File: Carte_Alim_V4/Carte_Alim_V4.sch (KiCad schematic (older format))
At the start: 61 parts, among them J1 BAT_IN, J10 12VC, J11 12VC, J12 12VC, J13 12VP, J14 12VP, J15 12VP, J16 12VP, J17 12VP, J18 12VP, J19 5VC, J2 BAT_IN, J20 5V_CAN, J21 5VC, J22 5V_CAN, J23 5VC, J24 5V_CAN, J25 5VC, J26 5V_CAN, J27 5VP, J28 5VP, J29 5VP, J3 MOT_OUT, J30 5VP, J31 5VP, J32 5VP, J4 MOT_OUT, J5 MOT_OUT, J6 MOT_OUT, J7 12VC, J8 12VC, J9 12VC, U1 LM2678S-5.0, U2 LM2678S-12

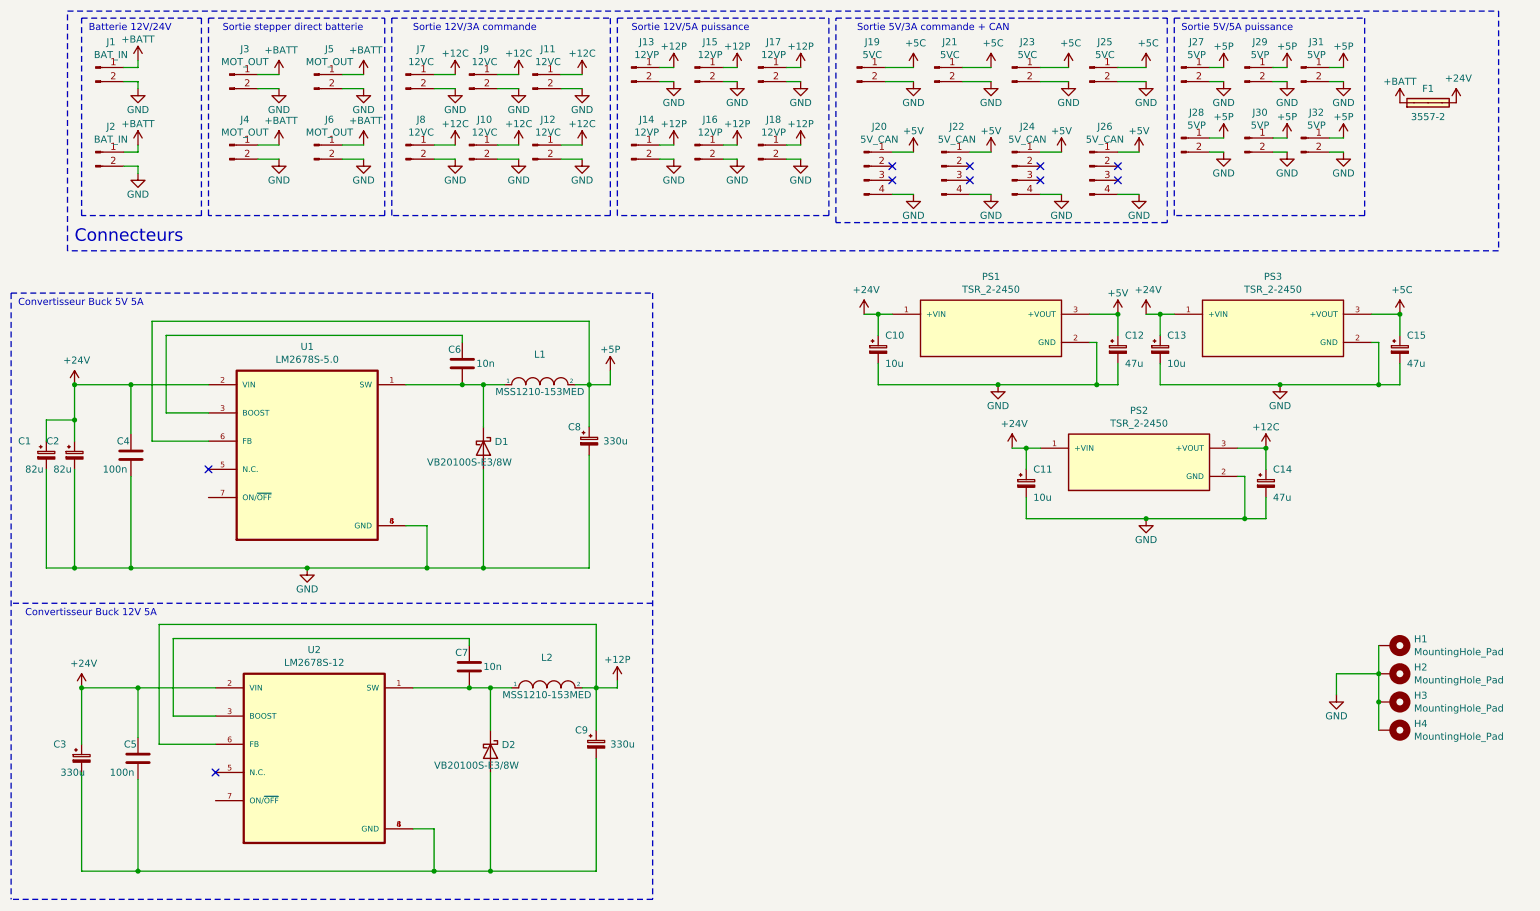
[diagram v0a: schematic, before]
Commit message: IO prete, Pompe finir sérigraphie, Alim+AX12 à faire
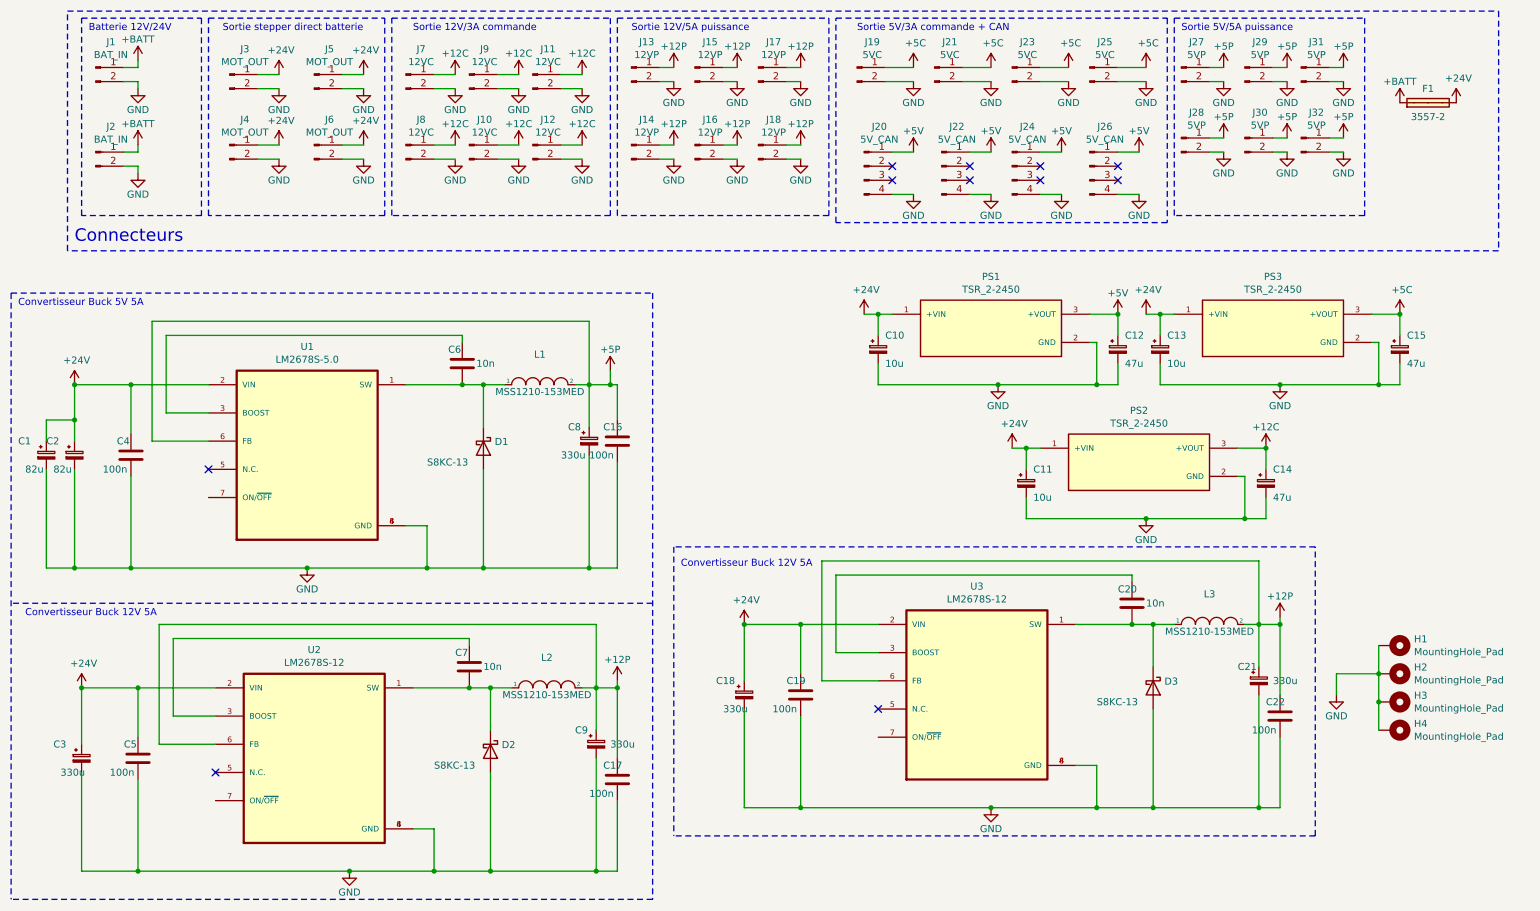
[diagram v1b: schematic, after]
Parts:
- added C16, C17, C19, C22: 100n, Capacitor_SMD:C_0805_2012Metric_Pad1.18x1.45mm_HandSolder, symbol Device:C
- added C18: 330u, Capacitor_SMD:CP_Elec_10x12.6, symbol Device:CP_Small
- added C20: 10n, Capacitor_SMD:C_0805_2012Metric_Pad1.18x1.45mm_HandSolder, symbol Device:C
- added C21: 330u, Capacitor_SMD:CP_Elec_8x6.2, symbol Device:CP_Small
- added D3: S8KC-13, Diode_SMD:D_SMC_Handsoldering, symbol Device:D_Schottky
- added L3: MSS1210-153MED, Inductor_SMD:L_12x12mm_H8mm, symbol pspice:INDUCTOR
- added U3: LM2678S-12, AREA_lib_composant:TO127P1435X464-8N, symbol AREA_composant:LM2678S-12
- D1, D2: value VB20100S-E3/8W -> S8KC-13; footprint Package_TO_SOT_SMD:TO-263-2_TabPin1 -> Diode_SMD:D_SMC_Handsoldering
- J20, J22, J24, J26: footprint AREA_lib_Connector:Wuerth_2mm_4pin_62000411622 -> AREA_lib_Connector:690367290476
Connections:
- net +12P: now also C17.1, C21.1, C22.1, L3.2, U3.6 (FB)
- net +24V: now also J3.1 (Pin_1), J4.1 (Pin_1), J5.1 (Pin_1), J6.1 (Pin_1), C18.1, C19.1, U3.2 (VIN)
- net +5P: now also C16.1
- net +BATT: no longer J3.1 (Pin_1), J4.1 (Pin_1), J5.1 (Pin_1), J6.1 (Pin_1)
- net GND: now also C3.2, C5.2, C9.2, D2.2 (A), U2.4 (GND), U2.8 (GND), C16.2, C17.2, C18.2, C19.2, C21.2, C22.2, D3.2 (A), U3.4 (GND), U3.8 (GND)
- new net: C20.2, D3.1 (K), L3.1, U3.1 (SW)
- new net: C20.1, U3.3 (BOOST)
- no-connect marks 10 -> 11
